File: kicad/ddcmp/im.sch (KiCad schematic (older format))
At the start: 8 parts, among them J2 RX, J3 TX, U2 max3089ecpd

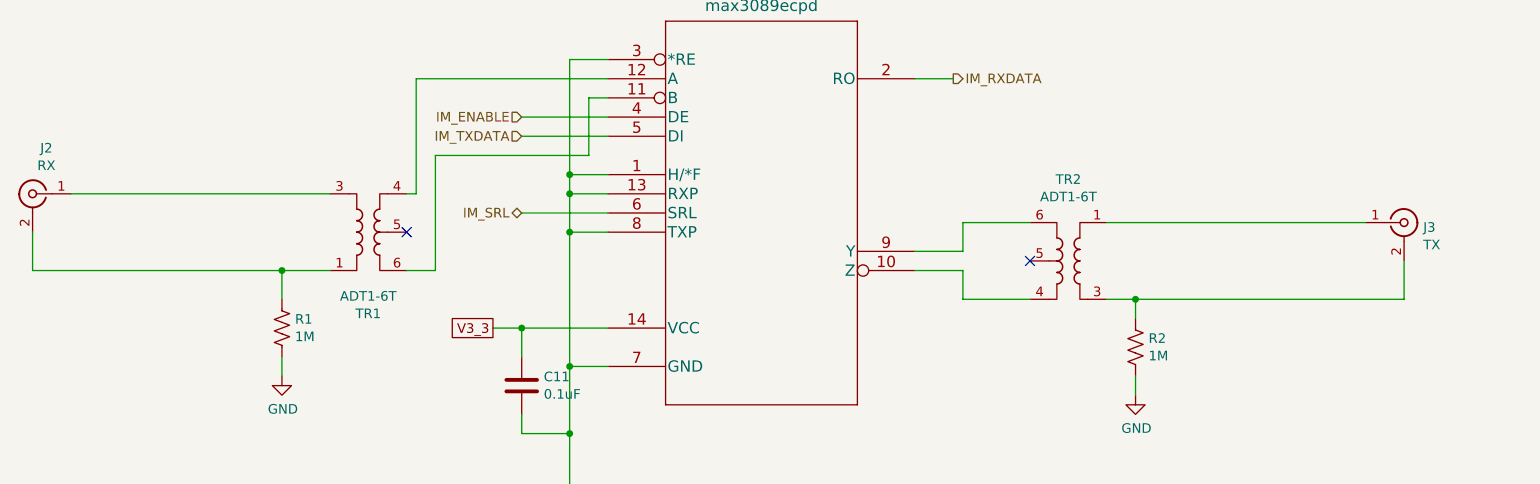
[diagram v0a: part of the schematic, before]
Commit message: Finish the connector hookups, to be verified carefully against DMR-11 schematics.
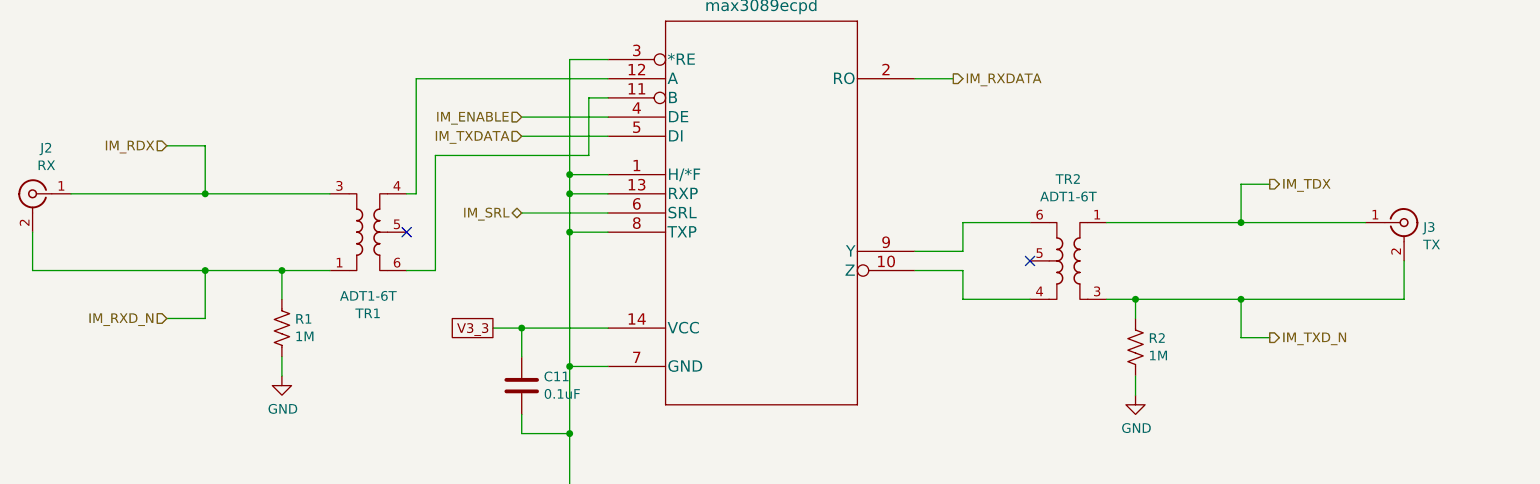
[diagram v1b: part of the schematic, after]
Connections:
- net IM_RXD_N: now reaches J2.2 (Ext), R1.1, TR1.1
- net IM_RDX: now reaches J2.1 (In), TR1.3
- net IM_TDX: now reaches J3.1 (In), TR2.1
- net IM_TXD_N: now reaches J3.2 (Ext), R2.1, TR2.3
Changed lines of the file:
@@
 $EndComp
 Wire Wire Line
-	8500 3050 7150 3050
+	8500 3050 7850 3050
 Wire Wire Line
 	7150 3450 7300 3450
@@
 Connection ~ 7300 3450
 Wire Wire Line
-	7300 3450 8700 3450
+	7300 3450 7850 3450
 Wire Wire Line
 	7300 3950 7300 3850
@@
 $EndComp
 Wire Wire Line
-	1750 2900 3100 2900
+	1750 2900 2450 2900
 Wire Wire Line
 	3100 3300 2850 3300
@@
 Connection ~ 2850 3300
 Wire Wire Line
-	2850 3300 1550 3300
+	2850 3300 2450 3300
 $Comp
 L ddcmp_symbols:C C11
@@
 Text GLabel 3950 3600 0    50   UnSpc ~ 0
 V3_3
+Wire Wire Line
+	7850 3050 7850 2850
+Wire Wire Line
+	7850 2850 8000 2850
+Connection ~ 7850 3050
+Wire Wire Line
+	7850 3050 7150 3050
+Wire Wire Line
+	7850 3450 7850 3650
+Wire Wire Line
+	7850 3650 8000 3650
+Connection ~ 7850 3450
+Wire Wire Line
+	7850 3450 8700 3450
+Text HLabel 8000 3650 2    50   Output ~ 0
+IM_TXD_N
+Text HLabel 8000 2850 2    50   Output ~ 0
+IM_TDX
+Wire Wire Line
+	2450 2900 2450 2650
+Wire Wire Line
+	2450 2650 2250 2650
+Connection ~ 2450 2900
+Wire Wire Line
+	2450 2900 3100 2900
+Wire Wire Line
+	2450 3300 2450 3550
+Wire Wire Line
+	2450 3550 2250 3550
+Connection ~ 2450 3300
+Wire Wire Line
+	2450 3300 1550 3300
+Text HLabel 2250 3550 0    50   Input ~ 0
+IM_RXD_N
+Text HLabel 2250 2650 0    50   Input ~ 0
+IM_RDX
 $EndSCHEMATC

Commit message: Complete schematic, PCB layout, and matching code.  Needs testing.
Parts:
- added R6: 240, ddcmp_parts:R_Axial_DIN0207_L6.3mm_D2.5mm_P10.16mm_Horizontal, symbol ddcmp_symbols:R_US
- added R7: 750, ddcmp_parts:R_Axial_DIN0207_L6.3mm_D2.5mm_P10.16mm_Horizontal, symbol ddcmp_symbols:R_US
- R1, R2: footprint ddcmp_parts:R_Axial_DIN0207_L6.3mm_D2.5mm_P7.62mm_Horizontal -> ddcmp_parts:R_Axial_DIN0207_L6.3mm_D2.5mm_P10.16mm_Horizontal
- U2: value max3089ecpd -> max3491ecpd; symbol ddcmp_symbols:max3089ecpd -> ddcmp_symbols:max3491ecpd
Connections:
- net IM_SRL is gone; now on net GND: U2.6 (GND)
- net GND: now also R7.2; no longer U2.1 (H/*F), U2.13 (RXP), U2.8 (TXP)
- net V3_3: now also U2.13 (VCC), R6.1
- net at TR1.5: now also R6.2, R7.1
- no-connect marks 2 -> 1
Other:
- moved on the sheet: C11, J2, J3, R1, R2, TR1, TR2

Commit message: Schematic and PCB modeling tweaks.
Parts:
- C11: Digikey 399-14010-1-ND​ -> (none); Digikey part (none) -> 399-14010-1-ND; Mfg Kemet -> (none); Mfg part C315C104M5U5TA7301 -> (none); Vendor (none) -> Kemet; Vendor part (none) -> C315C104M5U5TA7301
- J2, J3: Digikey part (none) -> WM20430-ND; Vendor (none) -> Molex; Vendor part (none) -> 0731713150
- R1, R2: Digikey part (none) -> 1.0MQBK-ND; Vendor (none) -> Yageo; Vendor part (none) -> CFR-25JB-52-1M
- R6: value 240 -> 270; Digikey part (none) -> 240QBK-ND; Vendor (none) -> Yageo; Vendor part (none) -> CFR-25JB-52-270R
- R7: Digikey part (none) -> 750QBK-ND; Vendor (none) -> Yageo; Vendor part (none) -> CFR-25JB-52-750R
- TR1, TR2: Digikey part (none) -> 3157-ADT1-6T+CT-ND; Vendor (none) -> Mini-Circuits; Vendor part (none) -> ADT1-6T+
- U2: Digikey part (none) -> MAX3491CPD+-ND; Vendor (none) -> Maxim; Vendor part (none) -> MAX3491CPD+
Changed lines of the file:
@@
 $Descr A4 11693 8268
 encoding utf-8
-Sheet 3 4
+Sheet 2 4
 Title "DDCMP Framer"
 Date "2021-05-17"
@@
 F 1 "max3491ecpd" H 5350 2481 60  0000 C CNN
 F 2 "ddcmp_parts:DIP-14_W7.62mm" H 5350 2440 60  0001 C CNN
-F 3 "" H 4550 2200 60  0000 C CNN
+F 3 "https://datasheets.maximintegrated.com/en/ds/MAX3483-MAX3491.pdf" H 4550 2200 60  0001 C CNN
+F 4 "MAX3491CPD+-ND" H 4550 2200 50  0001 C CNN "Digikey part"
+F 5 "Maxim" H 4550 2200 50  0001 C CNN "Vendor"
+F 6 "MAX3491CPD+" H 4550 2200 50  0001 C CNN "Vendor part"
 	1    4550 2200
 	1    0    0    -1
@@
 F 2 "ddcmp_parts:Mini-Circuits_CD637_H5.23mm" H 2800 2750 50  0001 C CNN
 F 3 "https://www.minicircuits.com/pdfs/ADT1-6T+.pdf" H 2800 3100 50  0001 C CNN
+F 4 "3157-ADT1-6T+CT-ND" H 0   0   50  0001 C CNN "Digikey part"
+F 5 "Mini-Circuits" H 0   0   50  0001 C CNN "Vendor"
+F 6 "ADT1-6T+" H 0   0   50  0001 C CNN "Vendor part"
 	1    2800 3100
 	1    0    0    -1
@@
 F 2 "ddcmp_parts:Mini-Circuits_CD637_H5.23mm" H 6950 2450 50  0001 C CNN
 F 3 "https://www.minicircuits.com/pdfs/ADT1-6T+.pdf" H 6950 2800 50  0001 C CNN
+F 4 "3157-ADT1-6T+CT-ND" H 0   0   50  0001 C CNN "Digikey part"
+F 5 "Mini-Circuits" H 0   0   50  0001 C CNN "Vendor"
+F 6 "ADT1-6T+" H 0   0   50  0001 C CNN "Vendor part"
 	1    6950 2800
 	-1   0    0    1
@@
 F 1 "TX" H 8800 2484 50  0000 L CNN
 F 2 "ddcmp_parts:BNC_Molex_J_RA_PCB" H 8700 2600 50  0001 C CNN
-F 3 " ~" H 8700 2600 50  0001 C CNN
+F 3 "https://www.molex.com/pdm_docs/sd/731000105_sd.pdf" H 8700 2600 50  0001 C CNN
+F 4 "WM20430-ND" H 0   0   50  0001 C CNN "Digikey part"
+F 5 "Molex" H 0   0   50  0001 C CNN "Vendor"
+F 6 "0731713150" H 0   0   50  0001 C CNN "Vendor part"
 	1    8700 2600
 	1    0    0    -1
@@
 F 2 "ddcmp_parts:R_Axial_DIN0207_L6.3mm_D2.5mm_P10.16mm_Horizontal" V 7340 3240 50  0001 C CNN
 F 3 "" H 7300 3250 50  0001 C CNN
+F 4 "1.0MQBK-ND" H 7300 3250 50  0001 C CNN "Digikey part"
+F 5 "Yageo" H 7300 3250 50  0001 C CNN "Vendor"
+F 6 "CFR-25JB-52-1M" H 7300 3250 50  0001 C CNN "Vendor part"
 	1    7300 3250
 	1    0    0    -1
@@
 F 2 "ddcmp_parts:R_Axial_DIN0207_L6.3mm_D2.5mm_P10.16mm_Horizontal" V 2540 3590 50  0001 C CNN
 F 3 "" H 2500 3600 50  0001 C CNN
+F 4 "1.0MQBK-ND" H 2500 3600 50  0001 C CNN "Digikey part"
+F 5 "Yageo" H 2500 3600 50  0001 C CNN "Vendor"
+F 6 "CFR-25JB-52-1M" H 2500 3600 50  0001 C CNN "Vendor part"
 	1    2500 3600
 	1    0    0    -1
@@
 F 1 "RX" H 1128 3047 50  0000 C CNN
 F 2 "ddcmp_parts:BNC_Molex_J_RA_PCB" H 1200 2900 50  0001 C CNN
-F 3 " ~" H 1200 2900 50  0001 C CNN
+F 3 "https://www.molex.com/pdm_docs/sd/731000105_sd.pdf" H 1200 2900 50  0001 C CNN
+F 4 "WM20430-ND" H 0   0   50  0001 C CNN "Digikey part"
+F 5 "Molex" H 0   0   50  0001 C CNN "Vendor"
+F 6 "0731713150" H 0   0   50  0001 C CNN "Vendor part"
 	1    1200 2900
 	-1   0    0    -1
@@
 F 2 "ddcmp_parts:C_Rect_L4.0mm_W2.5mm_P2.54mm" H 4138 3600 50  0001 C CNN
 F 3 "" H 4100 3750 50  0001 C CNN
-F 4 "399-14010-1-ND​" H 4100 3750 50  0001 C CNN "Digikey"
-F 5 "Kemet" H 4100 3750 50  0001 C CNN "Mfg"
-F 6 "C315C104M5U5TA7301" H 4100 3750 50  0001 C CNN "Mfg part"
+F 4 "399-14010-1-ND" H 4100 3750 50  0001 C CNN "Digikey part"
+F 5 "Kemet" H 4100 3750 50  0001 C CNN "Vendor"
+F 6 "C315C104M5U5TA7301" H 4100 3750 50  0001 C CNN "Vendor part"
+F 7 "399-14010-1-ND" H 4100 3750 50  0001 C CNN "Digikey part"
+F 8 "Kemet" H 4100 3750 50  0001 C CNN "Vendor"
+F 9 "C315C104M5U5TA7301" H 4100 3750 50  0001 C CNN "Vendor part"
 	1    4100 3750
 	1    0    0    -1
@@
 F 2 "ddcmp_parts:R_Axial_DIN0207_L6.3mm_D2.5mm_P10.16mm_Horizontal" V 3590 3740 50  0001 C CNN
 F 3 "" H 3550 3750 50  0001 C CNN
+F 4 "750QBK-ND" H 3550 3750 50  0001 C CNN "Digikey part"
+F 5 "Yageo" H 3550 3750 50  0001 C CNN "Vendor"
+F 6 "CFR-25JB-52-750R" H 3550 3750 50  0001 C CNN "Vendor part"
 	1    3550 3750
 	1    0    0    -1
@@
 P 3550 1800
 F 0 "R6" H 3618 1846 50  0000 L CNN
-F 1 "240" H 3618 1755 50  0000 L CNN
+F 1 "270" H 3618 1755 50  0000 L CNN
 F 2 "ddcmp_parts:R_Axial_DIN0207_L6.3mm_D2.5mm_P10.16mm_Horizontal" V 3590 1790 50  0001 C CNN
 F 3 "" H 3550 1800 50  0001 C CNN
+F 4 "240QBK-ND" H 3550 1800 50  0001 C CNN "Digikey part"
+F 5 "Yageo" H 3550 1800 50  0001 C CNN "Vendor"
+F 6 "CFR-25JB-52-270R" H 3550 1800 50  0001 C CNN "Vendor part"
 	1    3550 1800
 	1    0    0    -1

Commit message: Schematics and 3d model cleanups; first drafts of a lot of documentation.
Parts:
- R6: value 270 -> 51; Digikey part 240QBK-ND -> (none); Vendor Yageo -> (none); Vendor part CFR-25JB-52-270R -> (none)
- R7: value 750 -> 51; Digikey part 750QBK-ND -> (none); Vendor Yageo -> (none); Vendor part CFR-25JB-52-750R -> (none)
- TR1, TR2: value ADT1-6T -> TT1-6-X65+; footprint ddcmp_parts:Mini-Circuits_CD637_H5.23mm -> ddcmp_parts:Mini-Circuits_CD637_X65; symbol ddcmp_symbols:ADT1-6T -> ddcmp_symbols:TT1-6-X65+; Digikey part 3157-ADT1-6T+CT-ND -> (none); Vendor part ADT1-6T+ -> TT1-6-X65+
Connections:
- net GND: no longer R7.2
- net V3_3: no longer R6.1
- net at TR2.4, U2.10 (Z): now also R7.2
- net at TR1.6, U2.11 (B): now also R6.2
- net at TR1.4, U2.12 (A): now also R6.1
- net at TR2.6, U2.9 (Y): now also R7.1
- now unconnected: TR1.5
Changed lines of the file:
@@
 	6400 3000 6400 2850
 Wire Wire Line
-	6750 3000 6400 3000
-Wire Wire Line
-	6400 2600 6750 2600
+	6750 3000 6550 3000
+Wire Wire Line
+	6400 2600 6550 2600
 Wire Wire Line
 	6400 2750 6400 2600
@@
 $EndComp
 $Comp
-L ddcmp_symbols:ADT1-6T TR?
+L ddcmp_symbols:TT1-6-X65+ TR?
 U 1 1 60A5097C
 P 2800 3100
@@
 AR Path="/60A471E8/60A5097C" Ref="TR1"  Part="1"
 F 0 "TR1" H 2800 2675 50  0000 C CNN
-F 1 "ADT1-6T" H 2800 2766 50  0000 C CNN
-F 2 "ddcmp_parts:Mini-Circuits_CD637_H5.23mm" H 2800 2750 50  0001 C CNN
-F 3 "https://www.minicircuits.com/pdfs/ADT1-6T+.pdf" H 2800 3100 50  0001 C CNN
-F 4 "3157-ADT1-6T+CT-ND" H 0   0   50  0001 C CNN "Digikey part"
+F 1 "TT1-6-X65+" H 2800 2766 50  0000 C CNN
+F 2 "ddcmp_parts:Mini-Circuits_CD637_X65" H 2800 2750 50  0001 C CNN
+F 3 "https://www.minicircuits.com/pdfs/TT1-6-X65.pdf" H 2800 3100 50  0001 C CNN
+F 4 "" H 0   0   50  0001 C CNN "Digikey part"
 F 5 "Mini-Circuits" H 0   0   50  0001 C CNN "Vendor"
-F 6 "ADT1-6T+" H 0   0   50  0001 C CNN "Vendor part"
+F 6 "TT1-6-X65+" H 0   0   50  0001 C CNN "Vendor part"
 	1    2800 3100
 	1    0    0    -1
 $EndComp
 $Comp
-L ddcmp_symbols:ADT1-6T TR?
+L ddcmp_symbols:TT1-6-X65+ TR?
 U 1 1 60A50982
 P 6950 2800
@@
 AR Path="/60A471E8/60A50982" Ref="TR2"  Part="1"
 F 0 "TR2" H 6950 2375 50  0000 C CNN
-F 1 "ADT1-6T" H 6950 2466 50  0000 C CNN
-F 2 "ddcmp_parts:Mini-Circuits_CD637_H5.23mm" H 6950 2450 50  0001 C CNN
-F 3 "https://www.minicircuits.com/pdfs/ADT1-6T+.pdf" H 6950 2800 50  0001 C CNN
-F 4 "3157-ADT1-6T+CT-ND" H 0   0   50  0001 C CNN "Digikey part"
+F 1 "TT1-6-X65+" H 6950 2466 50  0000 C CNN
+F 2 "ddcmp_parts:Mini-Circuits_CD637_X65" H 6950 2450 50  0001 C CNN
+F 3 "https://www.minicircuits.com/pdfs/TT1-6-X65.pdf" H 6950 2800 50  0001 C CNN
+F 4 "" H 0   0   50  0001 C CNN "Digikey part"
 F 5 "Mini-Circuits" H 0   0   50  0001 C CNN "Vendor"
-F 6 "ADT1-6T+" H 0   0   50  0001 C CNN "Vendor part"
+F 6 "TT1-6-X65+" H 0   0   50  0001 C CNN "Vendor part"
 	1    6950 2800
 	-1   0    0    1
@@
 IM_TXDATA
 Wire Wire Line
-	3000 2900 3200 2900
+	3000 2900 3100 2900
 Wire Wire Line
 	3200 2900 3200 2300
 Wire Wire Line
-	3000 3300 3300 3300
+	3000 3300 3100 3300
 Wire Wire Line
 	3300 3300 3300 2400
@@
 Text HLabel 1900 2650 0    50   Input ~ 0
 IM_RDX
-$Comp
-L ddcmp_symbols:R_US R7
-U 1 1 60AA503A
-P 3550 3750
-F 0 "R7" H 3618 3796 50  0000 L CNN
-F 1 "750" H 3618 3705 50  0000 L CNN
-F 2 "ddcmp_parts:R_Axial_DIN0207_L6.3mm_D2.5mm_P10.16mm_Horizontal" V 3590 3740 50  0001 C CNN
-F 3 "" H 3550 3750 50  0001 C CNN
-F 4 "750QBK-ND" H 3550 3750 50  0001 C CNN "Digikey part"
-F 5 "Yageo" H 3550 3750 50  0001 C CNN "Vendor"
-F 6 "CFR-25JB-52-750R" H 3550 3750 50  0001 C CNN "Vendor part"
-	1    3550 3750
-	1    0    0    -1
-$EndComp
 Wire Wire Line
 	4550 3150 4100 3150
@@
 	4550 3050 4100 3050
 Connection ~ 4100 3050
-$Comp
-L ddcmp_symbols:R_US R6
-U 1 1 60AA4B02
-P 3550 1800
-F 0 "R6" H 3618 1846 50  0000 L CNN
-F 1 "270" H 3618 1755 50  0000 L CNN
-F 2 "ddcmp_parts:R_Axial_DIN0207_L6.3mm_D2.5mm_P10.16mm_Horizontal" V 3590 1790 50  0001 C CNN
-F 3 "" H 3550 1800 50  0001 C CNN
-F 4 "240QBK-ND" H 3550 1800 50  0001 C CNN "Digikey part"
-F 5 "Yageo" H 3550 1800 50  0001 C CNN "Vendor"
-F 6 "CFR-25JB-52-270R" H 3550 1800 50  0001 C CNN "Vendor part"
-	1    3550 1800
-	1    0    0    -1
-$EndComp
-Wire Wire Line
-	3550 1650 3550 1200
-Wire Wire Line
-	3000 3100 3550 3100
 Wire Wire Line
 	4450 4150 4450 4300
-Wire Wire Line
-	3550 3900 3550 4150
-Wire Wire Line
-	3550 4150 4100 4150
-Connection ~ 4100 4150
 Wire Wire Line
 	4100 3150 4100 3600
@@
 	4450 2200 4450 3250
 Wire Wire Line
-	3550 1950 3550 3100
-Wire Wire Line
 	4100 1200 4100 3050
 Wire Wire Line
@@
 Wire Wire Line
 	3300 2400 4550 2400
-Connection ~ 3550 1200
-Wire Wire Line
-	3550 1200 2800 1200
-Wire Wire Line
-	3550 1200 4100 1200
-Connection ~ 3550 3100
-Wire Wire Line
-	3550 3100 3550 3600
+Wire Wire Line
+	2800 1200 4100 1200
+$Comp
+L ddcmp_symbols:R_US R7
+U 1 1 60BD0969
+P 6550 2800
+F 0 "R7" H 6618 2846 50  0000 L CNN
+F 1 "51" H 6618 2755 50  0000 L CNN
+F 2 "ddcmp_parts:R_Axial_DIN0207_L6.3mm_D2.5mm_P10.16mm_Horizontal" V 6590 2790 50  0001 C CNN
+F 3 "" H 6550 2800 50  0001 C CNN
+	1    6550 2800
+	1    0    0    -1
+$EndComp
+$Comp
+L ddcmp_symbols:R_US R6
+U 1 1 60BD1A0F
+P 3100 3100
+F 0 "R6" H 3168 3146 50  0000 L CNN
+F 1 "51" H 3168 3055 50  0000 L CNN
+F 2 "ddcmp_parts:R_Axial_DIN0207_L6.3mm_D2.5mm_P10.16mm_Horizontal" V 3140 3090 50  0001 C CNN
+F 3 "" H 3100 3100 50  0001 C CNN
+	1    3100 3100
+	1    0    0    -1
+$EndComp
+Wire Wire Line
+	6550 2950 6550 3000
+Connection ~ 6550 3000
+Wire Wire Line
+	6550 3000 6400 3000
+Wire Wire Line
+	6550 2650 6550 2600
+Connection ~ 6550 2600
+Wire Wire Line
+	6550 2600 6750 2600
+Wire Wire Line
+	3100 2950 3100 2900
+Connection ~ 3100 2900
+Wire Wire Line
+	3100 2900 3200 2900
+Wire Wire Line
+	3100 3250 3100 3300
+Connection ~ 3100 3300
+Wire Wire Line
+	3100 3300 3300 3300
 $EndSCHEMATC

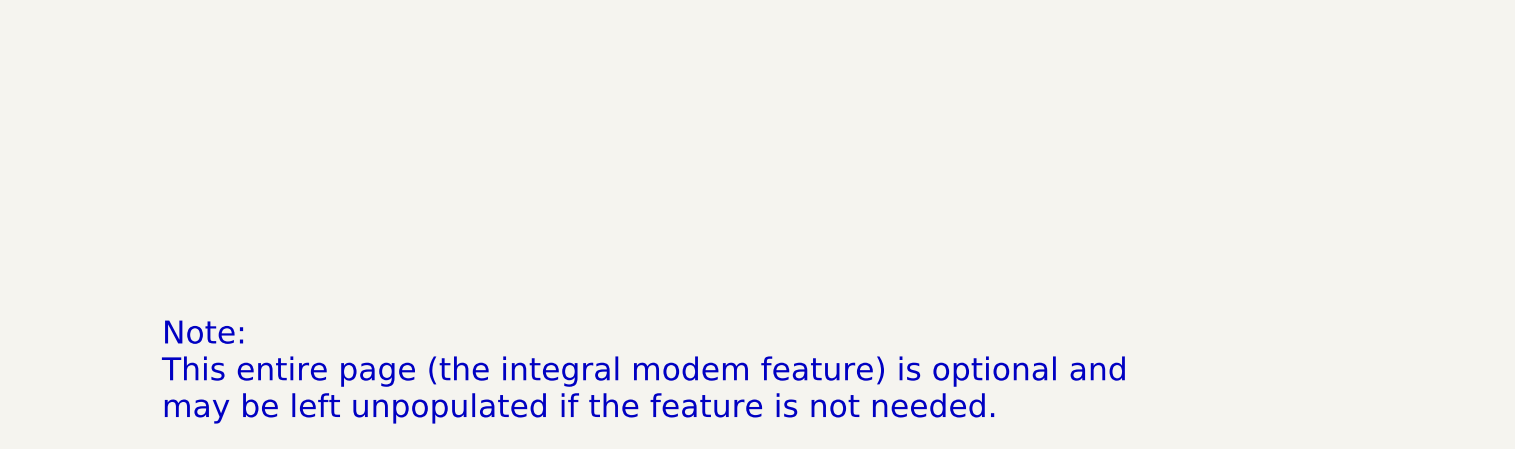
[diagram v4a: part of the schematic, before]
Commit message: Small schematics changes. Rewrite the integral modem receive demodulator state machine.
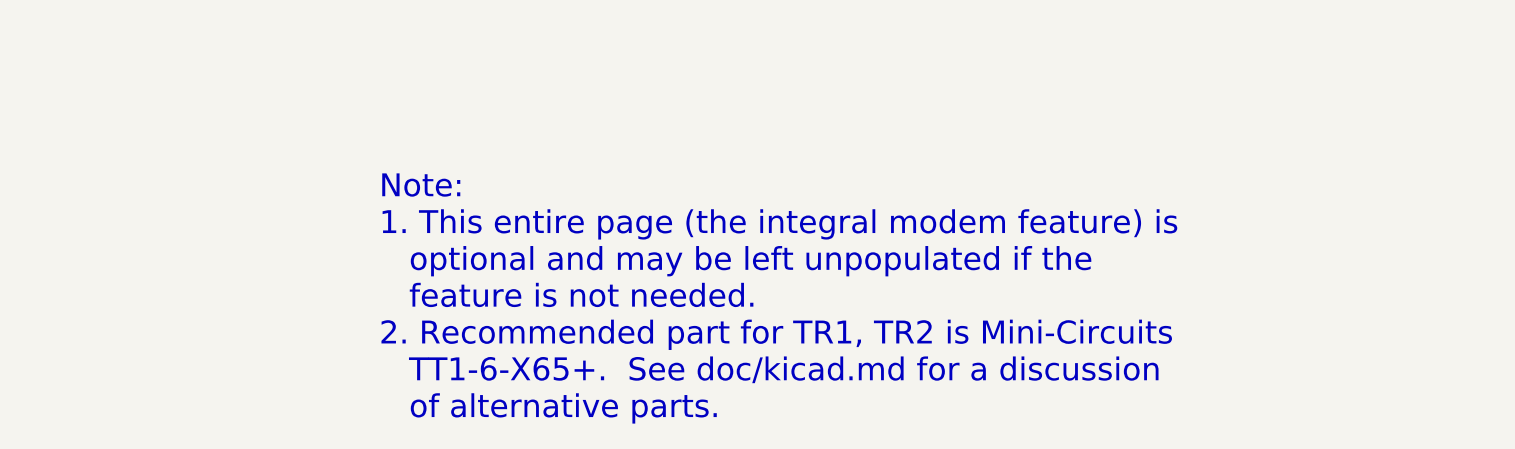
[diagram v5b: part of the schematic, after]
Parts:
- R6, R7: Digikey part (none) -> 51QBK-ND; Vendor (none) -> Yageo; Vendor part (none) -> CFR-25JB-52-51R
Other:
- note added: "Note:\n1. This entire page (the integral modem feature) is\n optional and may be left unpopulated if the\n feature is not needed.\n2. Recommended part for TR1, TR2 is Mini-Circuits\n TT1-6-X65+. See doc/kicad.md for a discussion\n of alternative parts."
- note removed: "Note:\nThis entire page (the integral modem feature) is optional and\nmay be left unpopulated if the feature is not needed."
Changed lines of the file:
@@
 F 1 "1M" H 7368 3205 50  0000 L CNN
 F 2 "ddcmp_parts:R_Axial_DIN0207_L6.3mm_D2.5mm_P10.16mm_Horizontal" V 7340 3240 50  0001 C CNN
-F 3 "" H 7300 3250 50  0001 C CNN
+F 3 "https://www.yageo.com/upload/media/product/products/datasheet/lr/Yageo_LR_CFR_1.pdf" H 7300 3250 50  0001 C CNN
 F 4 "1.0MQBK-ND" H 7300 3250 50  0001 C CNN "Digikey part"
 F 5 "Yageo" H 7300 3250 50  0001 C CNN "Vendor"
@@
 F 1 "1M" H 2568 3555 50  0000 L CNN
 F 2 "ddcmp_parts:R_Axial_DIN0207_L6.3mm_D2.5mm_P10.16mm_Horizontal" V 2540 3590 50  0001 C CNN
-F 3 "" H 2500 3600 50  0001 C CNN
+F 3 "https://www.yageo.com/upload/media/product/products/datasheet/lr/Yageo_LR_CFR_1.pdf" H 2500 3600 50  0001 C CNN
 F 4 "1.0MQBK-ND" H 2500 3600 50  0001 C CNN "Digikey part"
 F 5 "Yageo" H 2500 3600 50  0001 C CNN "Vendor"
@@
 F 1 "0.1uF" H 4215 3705 50  0000 L CNN
 F 2 "ddcmp_parts:C_Rect_L4.0mm_W2.5mm_P2.54mm" H 4138 3600 50  0001 C CNN
-F 3 "" H 4100 3750 50  0001 C CNN
+F 3 "https://content.kemet.com/datasheets/KEM_C1051_GOLDMAX_Z5U.pdf" H 4100 3750 50  0001 C CNN
 F 4 "399-14010-1-ND" H 4100 3750 50  0001 C CNN "Digikey part"
 F 5 "Kemet" H 4100 3750 50  0001 C CNN "Vendor"
@@
 	4100 4150 4450 4150
 Connection ~ 4450 4150
-Text Notes 6000 6250 0    100  ~ 0
-Note:\nThis entire page (the integral modem feature) is optional and\nmay be left unpopulated if the feature is not needed.
+Text Notes 6950 6250 0    100  ~ 0
+Note:\n1. This entire page (the integral modem feature) is\n   optional and may be left unpopulated if the\n   feature is not needed.\n2. Recommended part for TR1, TR2 is Mini-Circuits\n   TT1-6-X65+.  See doc/kicad.md for a discussion\n   of alternative parts.
 NoConn ~ 6750 2800
 Text GLabel 2800 1200 0    50   UnSpc ~ 0
@@
 F 1 "51" H 6618 2755 50  0000 L CNN
 F 2 "ddcmp_parts:R_Axial_DIN0207_L6.3mm_D2.5mm_P10.16mm_Horizontal" V 6590 2790 50  0001 C CNN
-F 3 "" H 6550 2800 50  0001 C CNN
+F 3 "https://www.yageo.com/upload/media/product/products/datasheet/lr/Yageo_LR_CFR_1.pdf" H 6550 2800 50  0001 C CNN
+F 4 "51QBK-ND" H 6550 2800 50  0001 C CNN "Digikey part"
+F 5 "Yageo" H 6550 2800 50  0001 C CNN "Vendor"
+F 6 "CFR-25JB-52-51R" H 6550 2800 50  0001 C CNN "Vendor part"
 	1    6550 2800
 	1    0    0    -1
@@
 F 1 "51" H 3168 3055 50  0000 L CNN
 F 2 "ddcmp_parts:R_Axial_DIN0207_L6.3mm_D2.5mm_P10.16mm_Horizontal" V 3140 3090 50  0001 C CNN
-F 3 "" H 3100 3100 50  0001 C CNN
+F 3 "https://www.yageo.com/upload/media/product/products/datasheet/lr/Yageo_LR_CFR_1.pdf" H 3100 3100 50  0001 C CNN
+F 4 "51QBK-ND" H 3100 3100 50  0001 C CNN "Digikey part"
+F 5 "Yageo" H 3100 3100 50  0001 C CNN "Vendor"
+F 6 "CFR-25JB-52-51R" H 3100 3100 50  0001 C CNN "Vendor part"
 	1    3100 3100
 	1    0    0    -1
